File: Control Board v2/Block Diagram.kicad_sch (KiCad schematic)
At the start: 0 parts

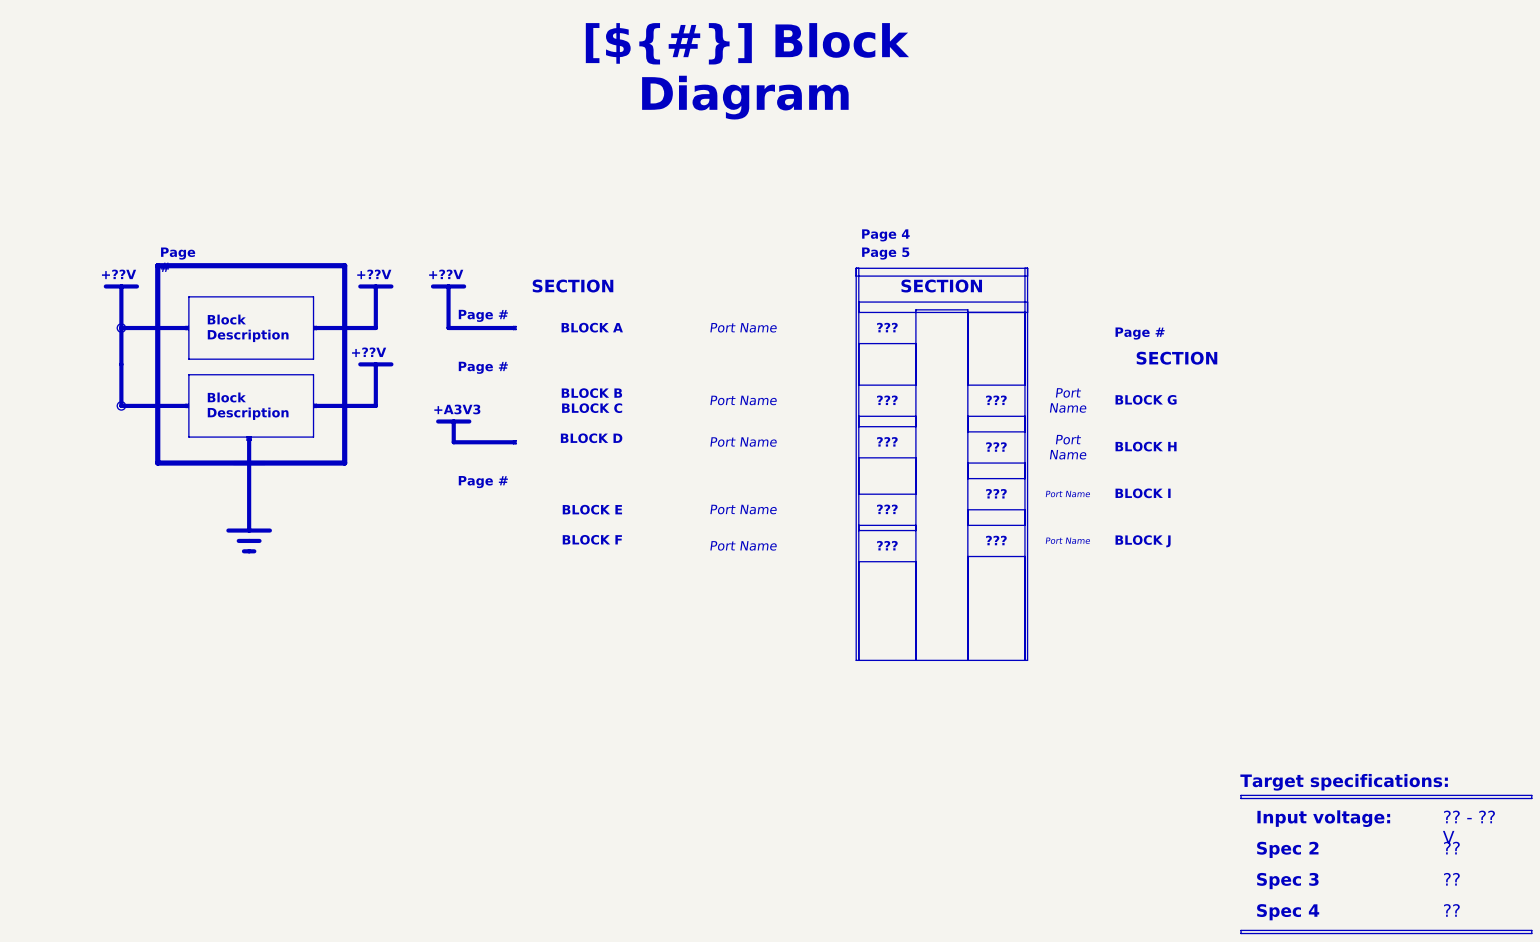
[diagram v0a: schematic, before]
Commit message: Finish preparing the template for v2 design
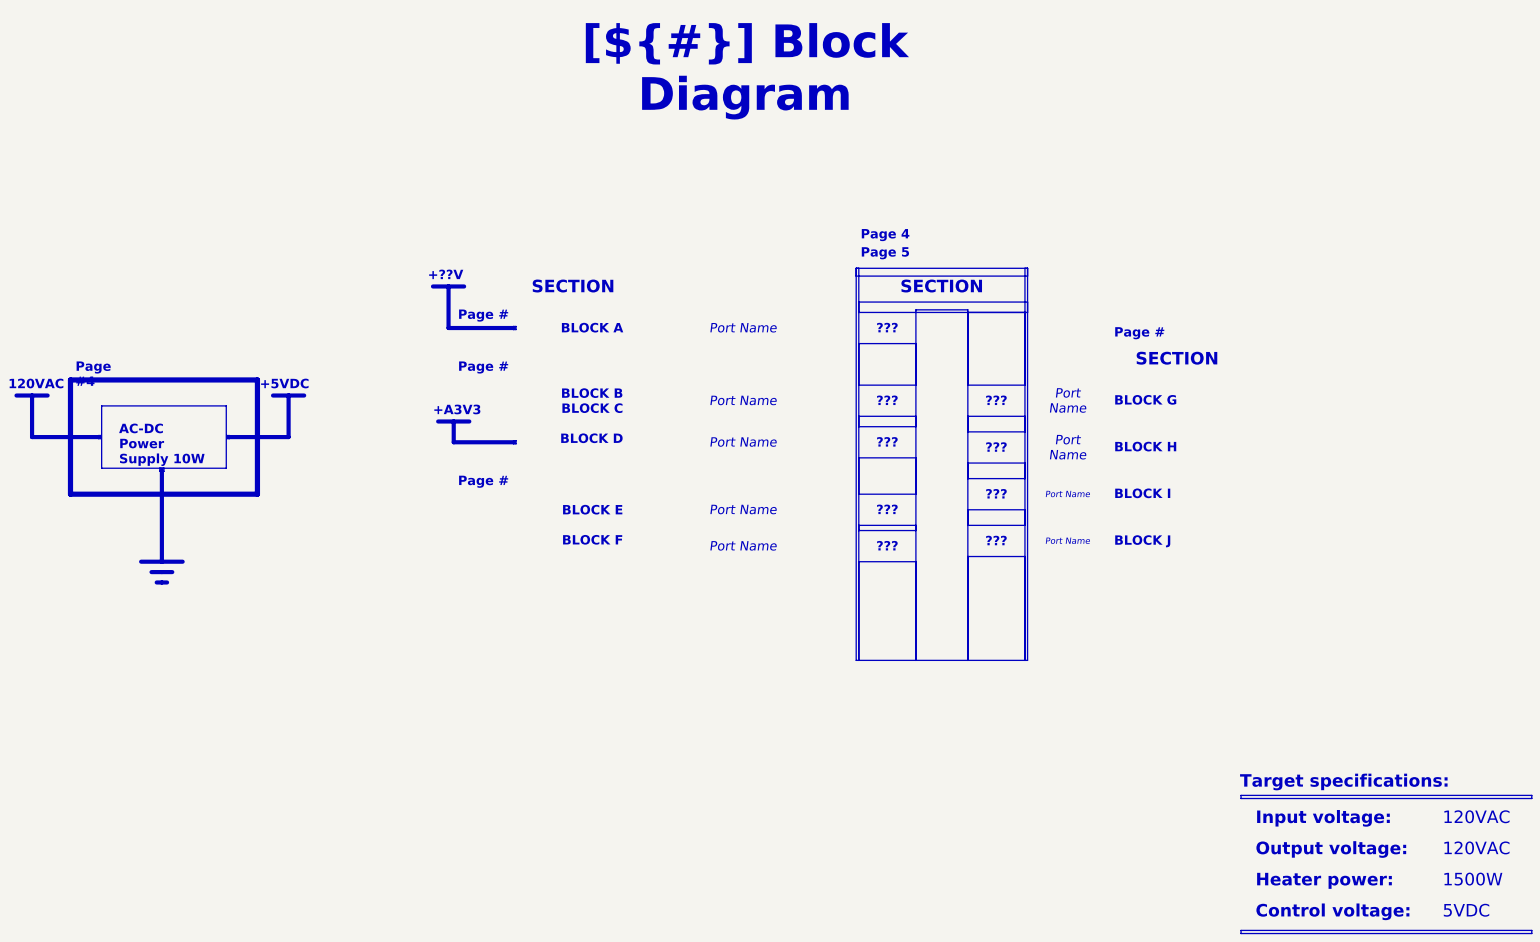
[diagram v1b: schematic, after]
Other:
- note added: "+5VDC"
- note added: "120VAC"
